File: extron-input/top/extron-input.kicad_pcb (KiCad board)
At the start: 2 copper layers, 114 x 37 mm, 22 parts, among them J1 SCART-F, J10 Conn_01x01, J11 RED_N, J12 BLUE, J13 SYNC, J2 RED, J3 GREEN, J4 BLUE, J5 SYNC, J6 PHOENIX, J7 SENSE, J8 Conn_01x01, J9 Conn_01x01, SW1 SW_DPDT_x2, U1 LM1881

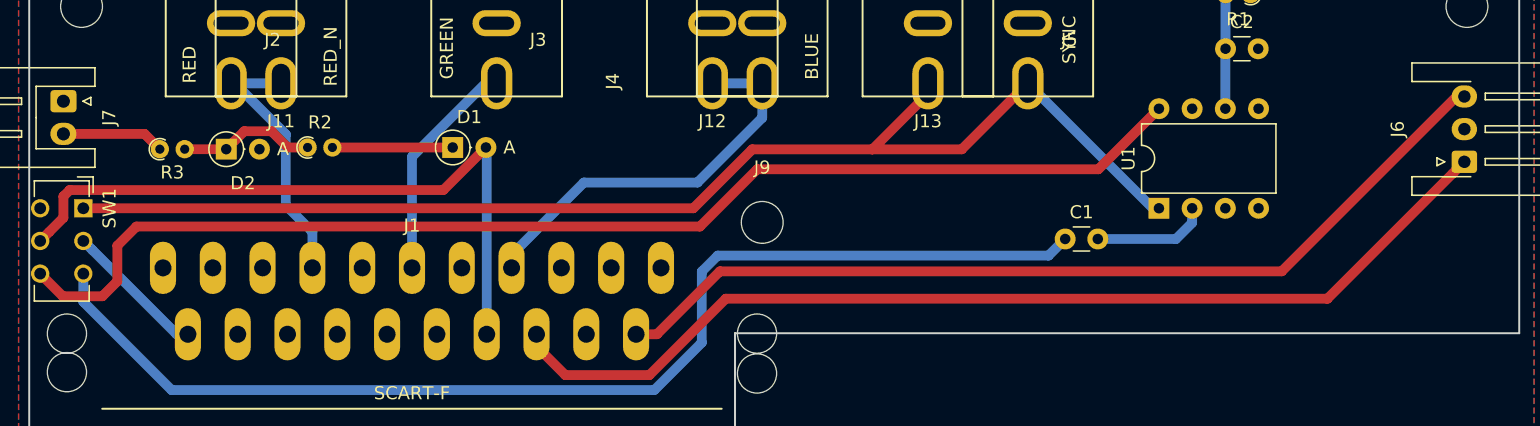
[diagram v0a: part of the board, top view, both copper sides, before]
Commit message: Added bottom board
Looks like I need to fix the schematic being in multiple places...
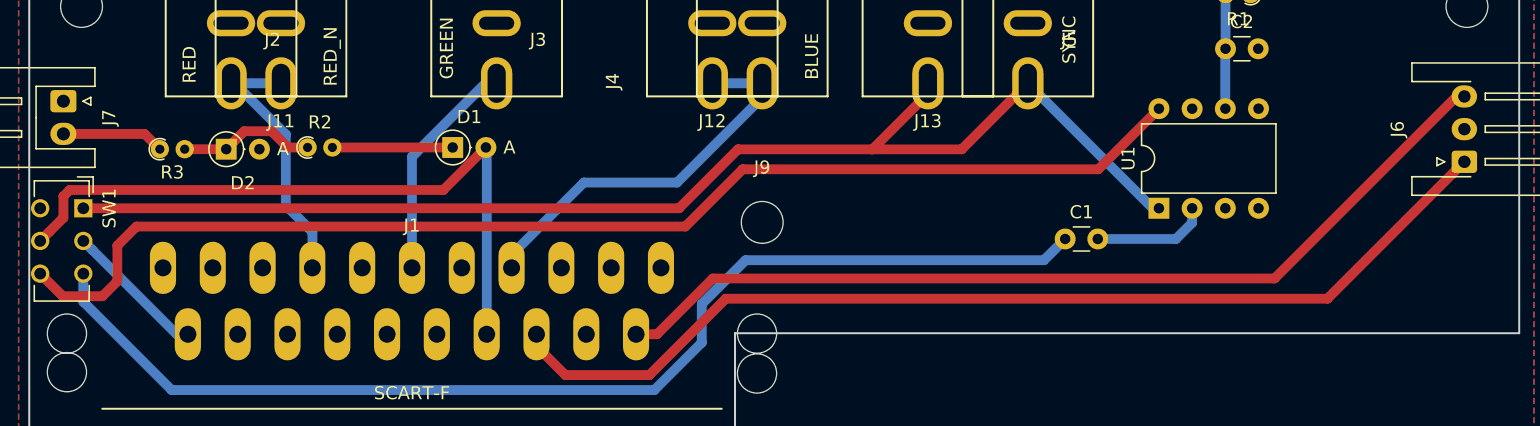
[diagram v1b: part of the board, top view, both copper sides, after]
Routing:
- net Net-(C1-Pad1): track 88.0 -> 86.6 mm
- net BLUE: track 31.0 -> 30.1 mm
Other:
- board text added: "v3.0pre"
- board text removed: "v2.2"
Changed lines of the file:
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@@
   )
   (setup
-    (last_trace_width 0.75)
+    (last_trace_width 0.254)
     (user_trace_width 0.5)
     (user_trace_width 0.75)
@@
   (gr_line (start 130 105) (end 190 105) (layer Edge.Cuts) (width 0.15))
   (gr_line (start 130 113) (end 130 105) (layer Edge.Cuts) (width 0.15))
-  (gr_text v2.2 (at 187.833 103.378) (layer B.SilkS)
+  (gr_text v3.0pre (at 186.4868 103.3272) (layer B.SilkS)
     (effects (font (size 1 1) (thickness 0.25)) (justify mirror))
   )
-  (gr_text "https://github.com/rattboi/extron-scart-adapter/\n" (at 159.385 102.997) (layer B.SilkS)
+  (gr_text "https://github.com/rattboi/extron-scart-adapter/\n" (at 159.385 103.3272) (layer B.SilkS)
     (effects (font (size 1 1) (thickness 0.15)) (justify mirror))
   )
@@
   (segment (start 162.433 95.4405) (end 161.9605 95.4405) (width 0.75) (layer B.Cu) (net 3))
   (segment (start 147.348 90.932) (end 152.4 85.88) (width 0.75) (layer F.Cu) (net 3))
-  (segment (start 80.137 95.4405) (end 126.8095 95.4405) (width 0.75) (layer F.Cu) (net 3))
-  (segment (start 126.8095 95.4405) (end 131.318 90.932) (width 0.75) (layer F.Cu) (net 3))
   (segment (start 144.76 86.68) (end 144.76 85.88) (width 0.75) (layer F.Cu) (net 3))
   (segment (start 140.508 90.932) (end 144.76 86.68) (width 0.75) (layer F.Cu) (net 3))
   (segment (start 140.462 90.932) (end 140.508 90.932) (width 0.75) (layer F.Cu) (net 3))
   (segment (start 140.462 90.932) (end 147.348 90.932) (width 0.75) (layer F.Cu) (net 3))
-  (segment (start 131.318 90.932) (end 140.462 90.932) (width 0.75) (layer F.Cu) (net 3))
+  (segment (start 130.2258 90.932) (end 140.462 90.932) (width 0.75) (layer F.Cu) (net 3))
+  (segment (start 80.137 95.4405) (end 125.7173 95.4405) (width 0.75) (layer F.Cu) (net 3))
+  (segment (start 125.7173 95.4405) (end 130.2258 90.932) (width 0.75) (layer F.Cu) (net 3))
   (segment (start 110.9065 85.88) (end 111.76 85.88) (width 0.75) (layer B.Cu) (net 4))
   (segment (start 105.283 99.999) (end 105.283 91.5035) (width 0.75) (layer B.Cu) (net 4))
   (segment (start 105.283 91.5035) (end 110.9065 85.88) (width 0.75) (layer B.Cu) (net 4))
+  (segment (start 128.26 85.88) (end 132.08 85.88) (width 0.75) (layer B.Cu) (net 5))
+  (segment (start 118.43 93.472) (end 112.903 98.999) (width 0.75) (layer B.Cu) (net 5))
+  (segment (start 125.5649 93.472) (end 118.43 93.472) (width 0.75) (layer B.Cu) (net 5))
+  (segment (start 132.08 85.88) (end 132.08 86.9569) (width 0.75) (layer B.Cu) (net 5))
   (segment (start 112.903 98.999) (end 112.903 99.999) (width 0.75) (layer B.Cu) (net 5))
-  (segment (start 118.43 93.472) (end 112.903 98.999) (width 0.75) (layer B.Cu) (net 5))
-  (segment (start 127.127 93.472) (end 118.43 93.472) (width 0.75) (layer B.Cu) (net 5))
-  (segment (start 132.08 85.88) (end 132.08 88.519) (width 0.75) (layer B.Cu) (net 5))
-  (segment (start 132.08 88.519) (end 127.127 93.472) (width 0.75) (layer B.Cu) (net 5))
-  (segment (start 128.26 85.88) (end 132.08 85.88) (width 0.75) (layer B.Cu) (net 5))
+  (segment (start 132.08 86.9569) (end 125.5649 93.472) (width 0.75) (layer B.Cu) (net 5))
   (segment (start 87.2755 105.079) (end 80.836999 98.640499) (width 0.75) (layer B.Cu) (net 12))
   (segment (start 80.836999 98.640499) (end 80.137 97.9405) (width 0.75) (layer B.Cu) (net 12))
   (segment (start 88.138 105.079) (end 87.2755 105.079) (width 0.75) (layer B.Cu) (net 12))
-  (segment (start 171.831 100.2665) (end 185.213 86.8845) (width 0.75) (layer F.Cu) (net 13))
-  (segment (start 128.8415 100.2665) (end 171.831 100.2665) (width 0.75) (layer F.Cu) (net 13))
+  (segment (start 185.213 86.8845) (end 185.801 86.8845) (width 0.75) (layer F.Cu) (net 13))
+  (segment (start 171.2849 100.8126) (end 185.213 86.8845) (width 0.75) (layer F.Cu) (net 13))
+  (segment (start 128.2954 100.8126) (end 171.2849 100.8126) (width 0.75) (layer F.Cu) (net 13))
   (segment (start 122.428 105.079) (end 124.029 105.079) (width 0.75) (layer F.Cu) (net 13))
-  (segment (start 185.213 86.8845) (end 185.801 86.8845) (width 0.75) (layer F.Cu) (net 13))
-  (segment (start 124.029 105.079) (end 128.8415 100.2665) (width 0.75) (layer F.Cu) (net 13))
+  (segment (start 124.029 105.079) (end 128.2954 100.8126) (width 0.75) (layer F.Cu) (net 13))
   (segment (start 184.902628 92.782872) (end 185.801 91.8845) (width 0.75) (layer F.Cu) (net 14))
   (segment (start 114.808 105.9942) (end 117.0178 108.204) (width 0.75) (layer F.Cu) (net 14))
@@
   (segment (start 162.2425 87.8205) (end 162.433 87.8205) (width 0.75) (layer B.Cu) (net 20))
   (segment (start 162.2425 87.8205) (end 162.433 87.8205) (width 0.254) (layer F.Cu) (net 20))
-  (segment (start 157.7975 92.456) (end 162.433 87.8205) (width 0.75) (layer F.Cu) (net 20))
-  (segment (start 131.699 92.456) (end 157.7975 92.456) (width 0.75) (layer F.Cu) (net 20))
+  (segment (start 126.1999 96.8375) (end 130.5814 92.456) (width 0.75) (layer F.Cu) (net 20))
   (segment (start 78.568 102.1715) (end 81.5975 102.1715) (width 0.75) (layer F.Cu) (net 20))
-  (segment (start 127.3175 96.8375) (end 131.699 92.456) (width 0.75) (layer F.Cu) (net 20))
   (segment (start 76.837 100.4405) (end 78.568 102.1715) (width 0.75) (layer F.Cu) (net 20))
   (segment (start 81.5975 102.1715) (end 82.7405 101.0285) (width 0.75) (layer F.Cu) (net 20))
+  (segment (start 82.7405 98.298) (end 84.201 96.8375) (width 0.75) (layer F.Cu) (net 20))
+  (segment (start 130.5814 92.456) (end 157.7975 92.456) (width 0.75) (layer F.Cu) (net 20))
   (segment (start 82.7405 101.0285) (end 82.7405 98.298) (width 0.75) (layer F.Cu) (net 20))
-  (segment (start 82.7405 98.298) (end 84.201 96.8375) (width 0.75) (layer F.Cu) (net 20))
-  (segment (start 84.201 96.8375) (end 127.3175 96.8375) (width 0.75) (layer F.Cu) (net 20))
+  (segment (start 157.7975 92.456) (end 162.433 87.8205) (width 0.75) (layer F.Cu) (net 20))
+  (segment (start 84.201 96.8375) (end 126.1999 96.8375) (width 0.75) (layer F.Cu) (net 20))
+  (segment (start 80.137 102.5906) (end 80.137 100.4405) (width 0.75) (layer B.Cu) (net 21))
+  (segment (start 153.6319 99.4156) (end 130.81 99.4156) (width 0.75) (layer B.Cu) (net 21))
   (segment (start 86.8934 109.347) (end 80.137 102.5906) (width 0.75) (layer B.Cu) (net 21))
-  (segment (start 80.137 102.5906) (end 80.137 100.4405) (width 0.75) (layer B.Cu) (net 21))
-  (segment (start 155.2575 97.79) (end 153.9875 99.06) (width 0.75) (layer B.Cu) (net 21))
-  (segment (start 128.6764 99.06) (end 127.4572 100.2792) (width 0.75) (layer B.Cu) (net 21))
-  (segment (start 127.4572 100.2792) (end 127.4572 105.7148) (width 0.75) (layer B.Cu) (net 21))
+  (segment (start 155.2575 97.79) (end 153.6319 99.4156) (width 0.75) (layer B.Cu) (net 21))
+  (segment (start 130.81 99.4156) (end 127.4572 102.7684) (width 0.75) (layer B.Cu) (net 21))
+  (segment (start 127.4572 105.7148) (end 123.825 109.347) (width 0.75) (layer B.Cu) (net 21))
+  (segment (start 127.4572 102.7684) (end 127.4572 105.7148) (width 0.75) (layer B.Cu) (net 21))
   (segment (start 123.825 109.347) (end 86.8934 109.347) (width 0.75) (layer B.Cu) (net 21))
-  (segment (start 153.9875 99.06) (end 128.6764 99.06) (width 0.75) (layer B.Cu) (net 21))
-  (segment (start 127.4572 105.7148) (end 123.825 109.347) (width 0.75) (layer B.Cu) (net 21))
   (segment (start 111.1885 104.8885) (end 110.998 105.079) (width 0.75) (layer B.Cu) (net 25))
   (segment (start 111 90.8496) (end 111 104.8885) (width 0.75) (layer B.Cu) (net 25))

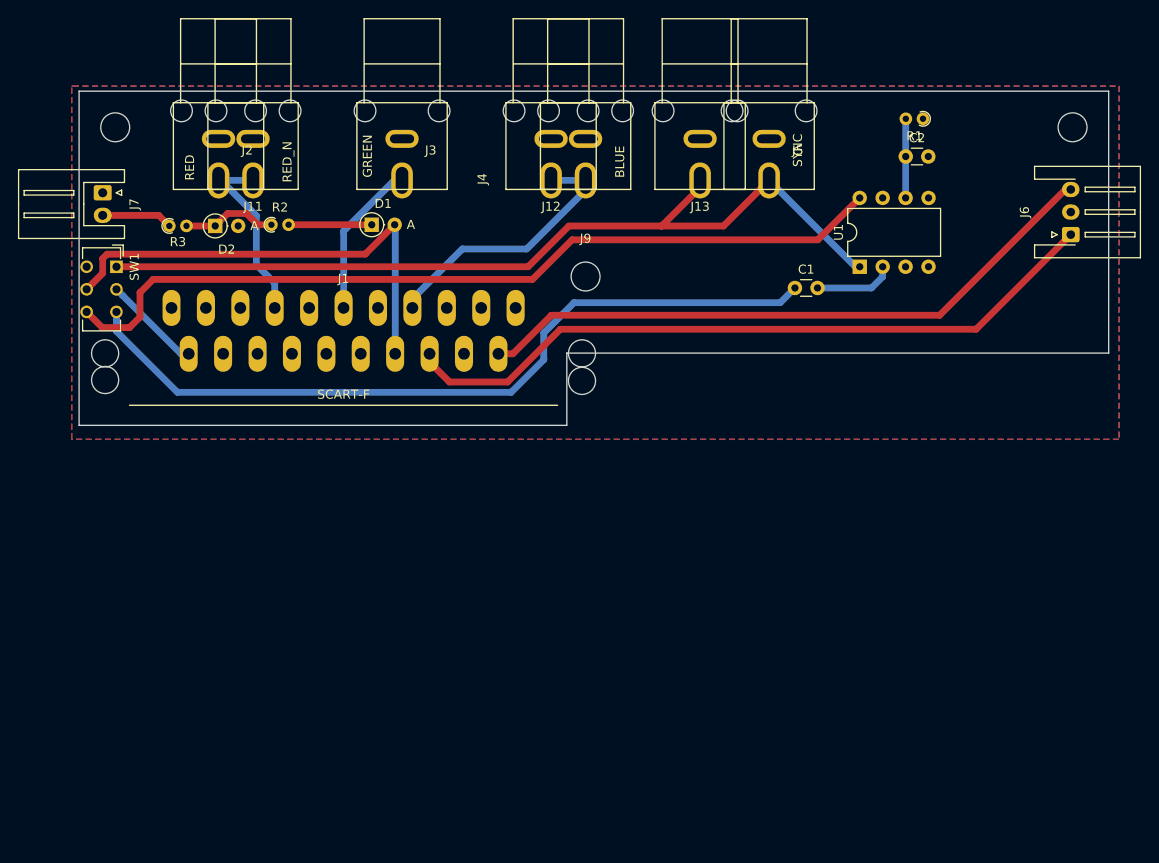
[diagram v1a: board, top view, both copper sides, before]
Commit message: Changed top to 45 degree scart insertion
* totally new concept here for me. I'm not super happy with the routing,
but I am more concerned about the mechanical layout right now, honestly.
I'm hoping that the track width being fairly wide will help the crap
routing.
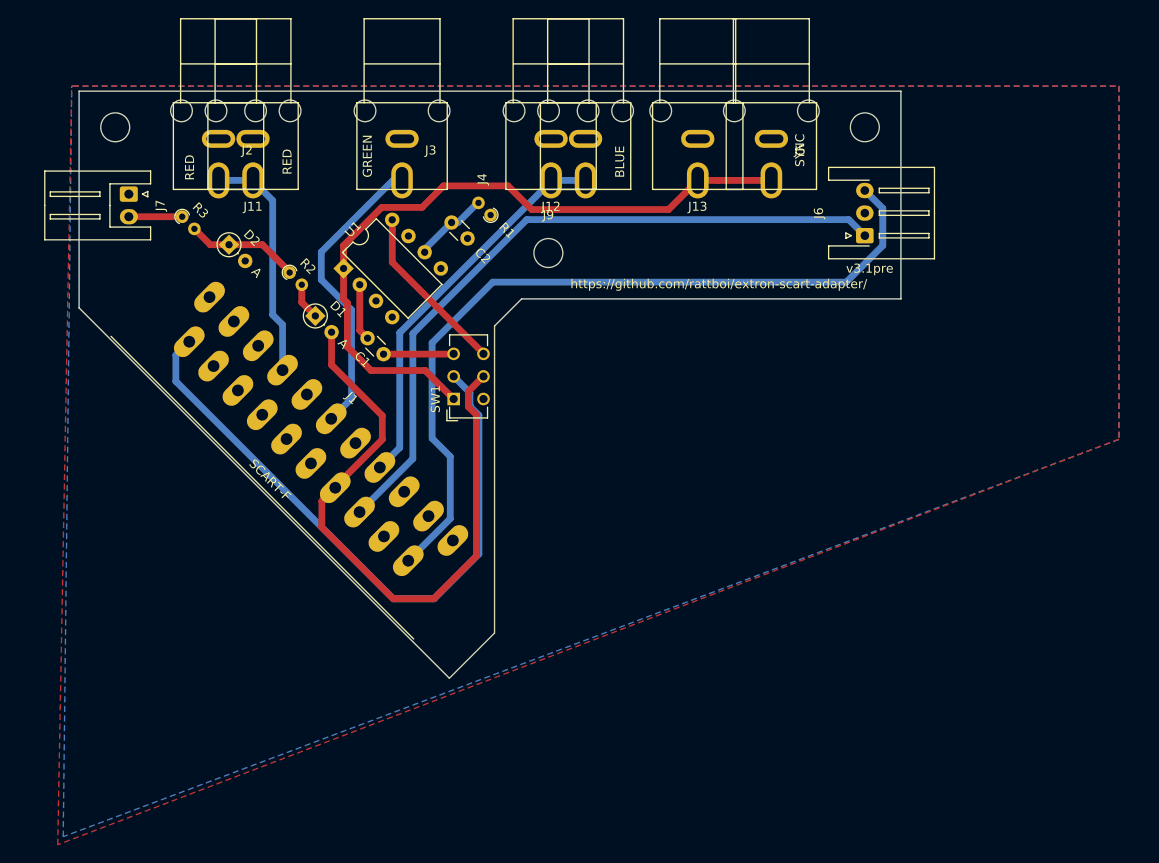
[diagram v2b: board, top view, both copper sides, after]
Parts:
- J11: value RED_N -> RED
- moved U1 57.2 mm to (105.3, 95.6), turned to 45 degrees
- moved C2 50.8 mm to (117.2, 90.5), turned to 315 degrees
- moved R1 49.0 mm to (121.6, 89.7), turned to 135 degrees
- moved C1 46.1 mm to (109.7, 105.1), turned to 135 degrees
- moved SW1 40.1 mm to (117.5, 110.1), turned to 90 degrees
- moved J8 23.0 mm to (163.0, 80.0)
- moved J6 22.8 mm to (163.0, 92.0)
- moved J1 11.9 mm to (100.3, 115.9), turned to 135 degrees
- moved D1 11.9 mm to (102.2, 100.9), turned to 315 degrees
- moved R2 5.67 mm to (99.3, 96.1), turned to 315 degrees
- moved J9 4.87 mm to (128.0, 93.9)
- moved J7 2.90 mm to (81.5, 87.4)
- moved D2 2.58 mm to (92.6, 93.0), turned to 315 degrees
- moved R3 1.76 mm to (87.4, 89.9), turned to 315 degrees
- moved J13 0.26 mm to (144.5, 81.3)
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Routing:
- net Net-(C1-Pad1): track 86.6 -> 8.19 mm
- net Net-(SW1-Pad6): track 94.2 -> 19.1 mm
- net Net-(J1-Pad20): track 11.0 -> 71.5 mm
- net SYNC: track 98.4 -> 80.0 mm
- net SENSE: track 52.4 -> 70.0 mm
- net Net-(J1-Pad2): track 70.9 -> 88.2 mm
- net GREEN: track 17.3 -> 33.9 mm
- net BLUE: track 30.1 -> 44.5 mm
- net RED: track 20.7 -> 26.5 mm
- net Net-(D1-Pad1): track 9.20 -> 4.08 mm
- net Net-(C1-Pad2): track 8.84 -> 6.28 mm
- net Net-(D2-Pad1): track 10.5 -> 12.6 mm
- net Net-(J7-Pad2): track 7.86 -> 5.91 mm
- net Net-(J1-Pad6): track 79.6 -> 78.2 mm
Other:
- board size 114 x 37 mm -> 91 x 65 mm
- board text added: "v3.1pre"
- board text removed: "v3.0pre"

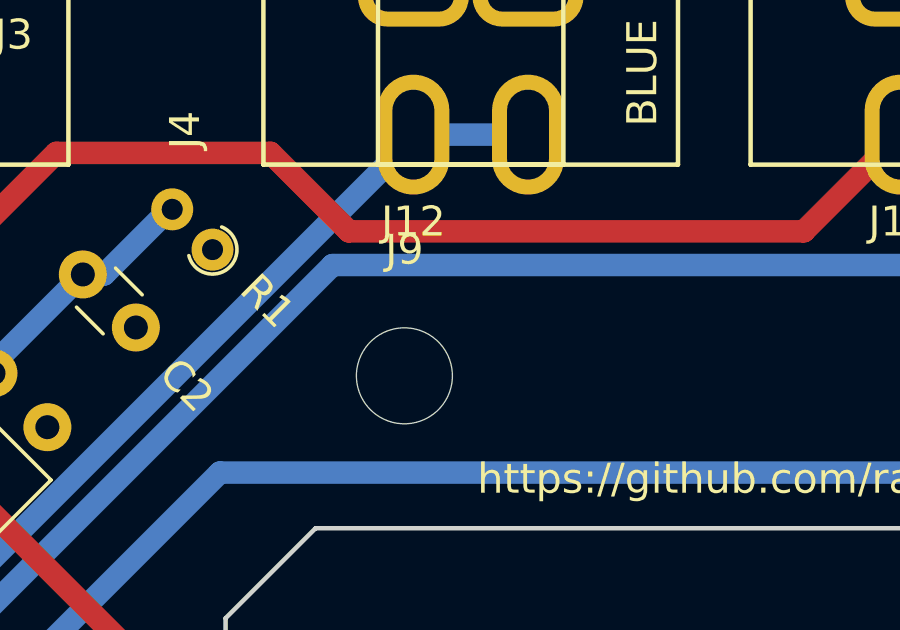
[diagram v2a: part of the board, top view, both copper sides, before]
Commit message: Bottom board is now done(ish)
I've also aligned the mounting holes between the boards
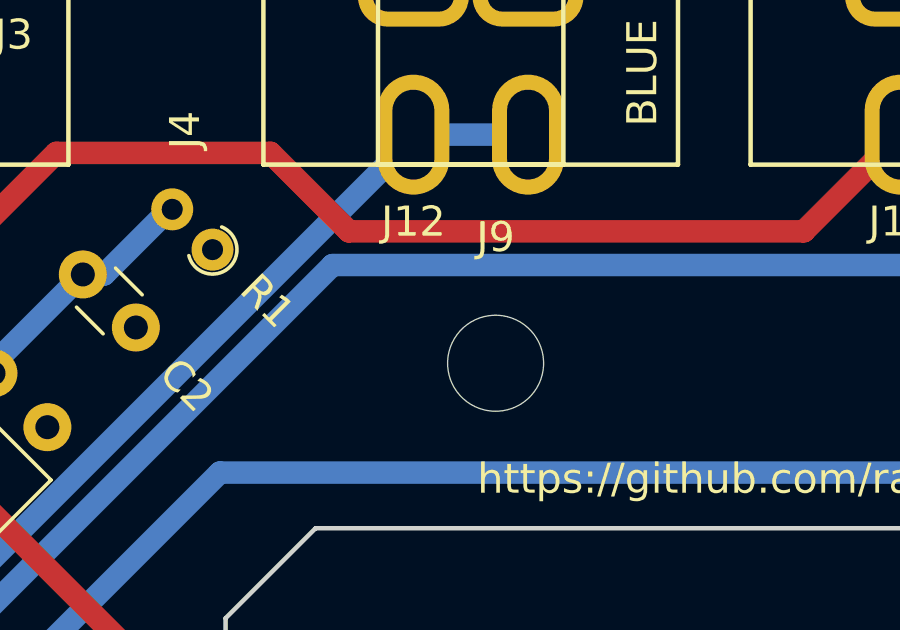
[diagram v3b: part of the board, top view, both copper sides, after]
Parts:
- moved J9 3.07 mm to (131.0, 93.5)
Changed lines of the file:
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@@
   )
   (setup
-    (last_trace_width 0.75)
+    (last_trace_width 0.254)
     (user_trace_width 0.5)
     (user_trace_width 0.75)
@@
   )
   (module MountingHole:MountingHole_3.2mm_M3 (layer F.Cu)
-    (at 127.96012 93.91904)
+    (at 131 93.5)
     (descr "Mounting Hole 3.2mm, no annular, M3")
     (tags "mounting hole 3.2mm no annular m3")
